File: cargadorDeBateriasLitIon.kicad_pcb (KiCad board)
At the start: 2 copper layers, 17 x 12 mm, 13 parts, among them Q1 2N7002, Q2 2N7002, U1 MCP73831-2, U2 AP9101C

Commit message: PCB version 1, falta probar
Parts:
- added G***: LOGO, MSS_Devices:logo-mr_solder_7.8x3.6mm, B.Cu at (149.0, 105.3)
- added J1: IN+, TestPoint:TestPoint_THTPad_1.5x1.5mm_Drill0.7mm, F.Cu at (140.5, 114.0)
- added J2: IN-, TestPoint:TestPoint_THTPad_1.5x1.5mm_Drill0.7mm, F.Cu at (140.5, 103.0)
- added J3: OUT+, TestPoint:TestPoint_THTPad_1.5x1.5mm_Drill0.7mm, F.Cu at (158.0, 106.0)
- added J4: B+, TestPoint:TestPoint_THTPad_1.5x1.5mm_Drill0.7mm, F.Cu at (158.0, 103.0)
- added J5: B-, TestPoint:TestPoint_THTPad_1.5x1.5mm_Drill0.7mm, F.Cu at (158.0, 111.0)
- added J6: OUT-, TestPoint:TestPoint_THTPad_1.5x1.5mm_Drill0.7mm, F.Cu at (158.0, 114.0)
- moved C1 5.44 mm to (145.7, 112.4), turned to 180 degrees
- moved R2 3.83 mm to (146.5, 105.4), turned to 0 degrees
- moved R1 3.22 mm to (141.6, 108.4), turned to 270 degrees
- moved U2 2.76 mm to (150.7, 108.1)
- moved R3 2.66 mm to (153.3, 107.9)
- moved R4 1.83 mm to (153.7, 105.2)
- moved C3 1.65 mm to (150.4, 105.2)
- moved Q2 1.51 mm to (150.5, 112.1), turned to 270 degrees
- moved Q1 1.29 mm to (154.2, 112.1), turned to 270 degrees
- moved D1 0.88 mm to (146.5, 110.8)
- moved C2 0.84 mm to (143.3, 110.8)
- moved C4 0.67 mm to (143.3, 108.4)
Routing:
- net /B+: track 0.00 -> 24.5 mm
- net /B-: track 0.00 -> 20.5 mm
- net /IN+: track 0.00 -> 10.8 mm
- net Net-(D1-Pad1): track 0.00 -> 9.90 mm
- net GND: track 0.00 -> 8.87 mm, vias 0 -> 1
- net Net-(Q1-Pad3): track 0.00 -> 7.45 mm
- net Net-(R1-Pad1): track 0.00 -> 4.35 mm
- net Net-(Q1-Pad1): track 0.00 -> 4.22 mm
- net Net-(Q1-Pad2): track 0.00 -> 4.02 mm
- net Net-(C3-Pad1): track 0.00 -> 3.61 mm
- net Net-(Q2-Pad1): track 0.00 -> 2.48 mm
- net Net-(R3-Pad2): track 0.00 -> 1.75 mm
- net Net-(R2-Pad2): track 0.00 -> 1.75 mm
- added copper zone on B.Cu, net GND
- added copper zone on F.Cu, net GND
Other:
- board size 17 x 12 mm -> 19.5 x 13 mm
- board text added: "B+"
- board text added: "B-"
- board text added: "IN+"
- board text added: "IN-"
- board text added: "OUT+"
- board text added: "OUT-"

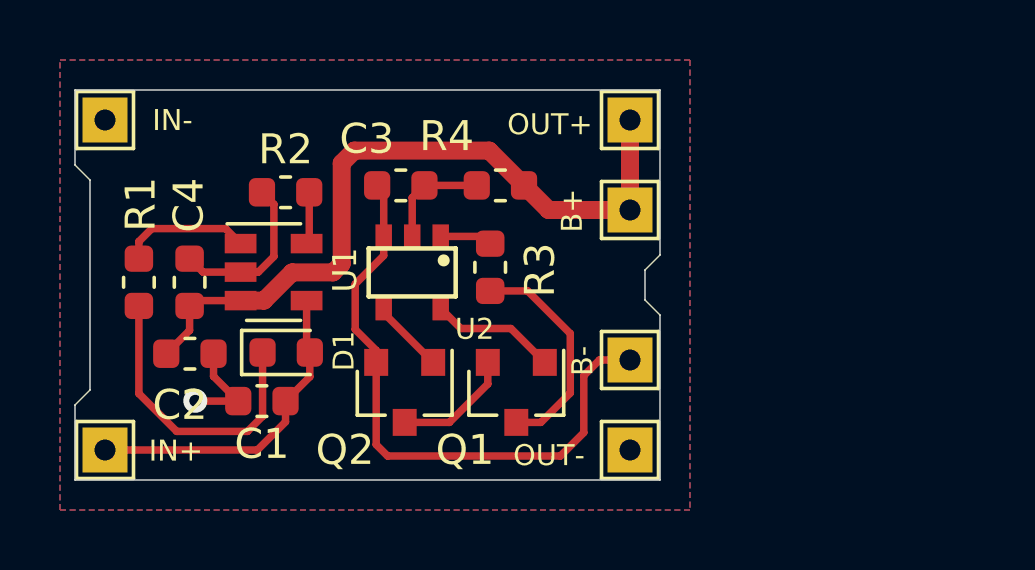
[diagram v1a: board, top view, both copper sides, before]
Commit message: generando gerber, faltan optimizar mas las pistas
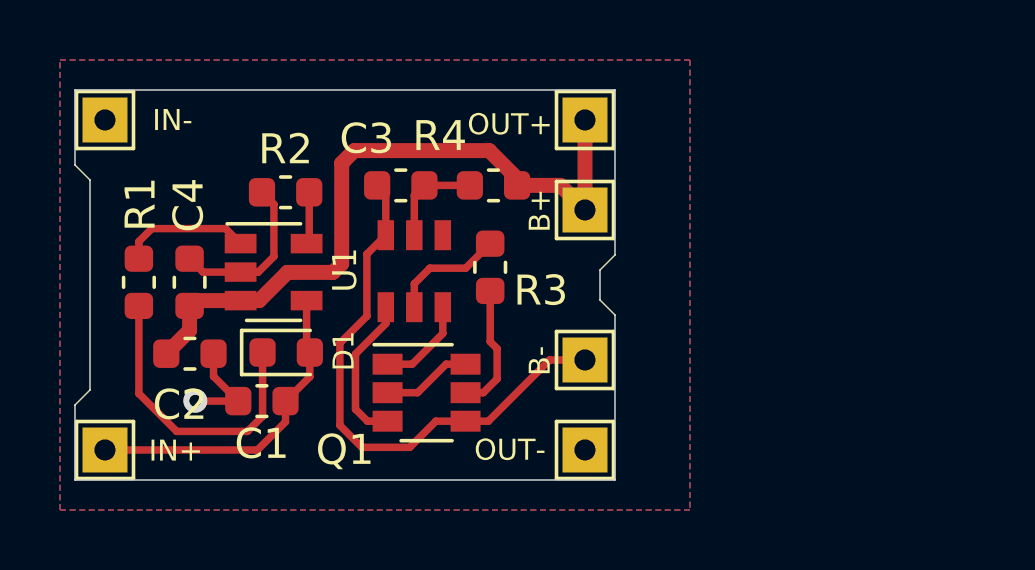
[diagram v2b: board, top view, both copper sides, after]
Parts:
- removed Q2: 2N7002, Package_TO_SOT_SMD:SOT-23
- Q1: value 2N7002 -> FDC6401N; footprint Package_TO_SOT_SMD:SOT-23 -> Package_TO_SOT_SMD:SuperSOT-6
- U1: value MCP73831-2 -> MCP73831
- U2: value AP9101C -> AP9101CK6; footprint MSS_Devices:SOT25 -> MSS_Devices:SOT26
- moved Q1 2.99 mm to (151.2, 112.1), turned to 0 degrees
- moved J3 1.50 mm to (156.5, 106.0)
- moved J4 1.50 mm to (156.5, 103.0)
- moved J5 1.50 mm to (156.5, 111.0)
- moved J6 1.50 mm to (156.5, 114.0)
- moved G*** 1.35 mm to (148.3, 106.5)
- moved R4 0.23 mm to (153.4, 105.2)
- moved U2 0.08 mm to (150.8, 108.0), turned to 0 degrees
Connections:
- R3 pad 1: Net-(Q1-Pad3) -> Net-(Q1-Pad5)
- U2 pad 1: Net-(R3-Pad2) -> Net-(Q1-Pad3)
- U2 pad 2: Net-(C3-Pad1) -> Net-(R3-Pad2)
- U2 pad 3: /B- -> Net-(Q1-Pad1)
- U2 pad 4: Net-(Q2-Pad1) -> (no net)
- U2 pad 5: Net-(Q1-Pad1) -> Net-(C3-Pad1)
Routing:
- net Net-(Q1-Pad5): track 0.00 -> 4.27 mm
- net Net-(Q2-Pad1): track 2.48 -> 0.00 mm
- net Net-(Q1-Pad3): track 7.45 -> 5.05 mm
- net Net-(R3-Pad2): track 1.75 -> 3.86 mm
- net /B-: track 20.5 -> 18.4 mm
- net /B+: track 24.5 -> 23.2 mm
- net Net-(Q1-Pad1): track 4.22 -> 3.14 mm
- net Net-(Q1-Pad2): track 4.02 -> 2.99 mm
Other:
- board size 19.5 x 13 mm -> 18 x 13 mm
- board text added: "MAYKOLREY.COM"

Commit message: agregando fuente de voltaje constante a 5V
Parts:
- removed G***: LOGO, MSS_Devices:logo-mr_solder_7.8x3.6mm
- added C5: 4.7nF, Capacitor_SMD:C_0805_2012Metric, F.Cu at (164.8, 111.5)
- added D2: SM5819PL-TP, Diode_SMD:D_SOD-123F, F.Cu at (164.0, 107.2)
- added L1: 10uH, MSS_Devices:L_Bourns_SDR0403, F.Cu at (159.5, 106.0)
- added R5: 100K, Resistor_SMD:R_0603_1608Metric, F.Cu at (162.0, 110.5)
- added R6: 33K, Resistor_SMD:R_0603_1608Metric, F.Cu at (162.0, 112.2)
- added U3: MIC2251, Package_TO_SOT_SMD:SOT-23-5, F.Cu at (157.8, 111.5)
- C4: value 100nF -> 10uF; footprint Capacitor_SMD:C_0603_1608Metric -> Capacitor_SMD:C_0805_2012Metric
- moved J6 12.0 mm to (168.0, 110.5)
- moved J5 11.9 mm to (168.0, 114.0)
- moved C4 11.7 mm to (154.7, 110.9)
- moved J3 11.5 mm to (168.0, 106.5)
- moved J4 11.5 mm to (168.0, 103.0)
- moved R1 6.81 mm to (147.7, 111.5)
- moved C2 5.83 mm to (144.6, 105.1)
- moved R2 2.94 mm to (147.7, 108.1), turned to 270 degrees
- moved J1 2.06 mm to (142.5, 113.5)
- moved J2 2.00 mm to (142.5, 103.0)
- moved D1 1.24 mm to (145.3, 110.7), turned to 180 degrees
- moved U1 1.13 mm to (145.0, 107.9), turned to 270 degrees
- moved R3 0.91 mm to (154.2, 107.6), turned to 270 degrees
- moved C1 0.44 mm to (145.3, 112.3), turned to 0 degrees
- turned U2 to 180 degrees
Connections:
- net /IN+ renamed VDD
- J3 pad 1: /B+ -> /STEP-UP/VOUT
- Q1 pad 2: Net-(Q1-Pad2) -> GND
- Q1 pad 4: /B- -> Net-(Q1-Pad4)
- Q1 pad 5: Net-(Q1-Pad5) -> /B-
- Q1 pad 6: Net-(Q1-Pad2) -> Net-(Q1-Pad4)
- R3 pad 1: Net-(Q1-Pad5) -> Net-(R3-Pad1)
- R3 pad 2: Net-(R3-Pad2) -> GND
- U2 pad 1: Net-(Q1-Pad3) -> Net-(R3-Pad1)
- U2 pad 2: Net-(R3-Pad2) -> Net-(C3-Pad1)
- U2 pad 3: Net-(Q1-Pad1) -> /B-
- U2 pad 4: (no net) -> Net-(Q1-Pad1)
- U2 pad 5: Net-(C3-Pad1) -> Net-(Q1-Pad3)
- U2 pad 6: /B- -> (no net)
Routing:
- net GND: track 8.87 -> 30.5 mm, vias 1 -> 4
- net Net-(D2-Pad2): track 0.00 -> 10.9 mm, vias 0 -> 4
- net /STEP-UP/VOUT: track 0.00 -> 9.50 mm
- net /B-: track 18.4 -> 27.3 mm
- net Net-(D1-Pad1): track 9.90 -> 2.27 mm
- net /B+: track 23.2 -> 29.0 mm, vias 0 -> 4
- net Net-(Q1-Pad5): track 4.27 -> 0.00 mm
- net Net-(R1-Pad1): track 4.35 -> 8.52 mm
- net Net-(R5-Pad2): track 0.00 -> 4.13 mm
- net Net-(R3-Pad2): track 3.86 -> 0.00 mm
- net Net-(Q1-Pad4): track 0.00 -> 3.31 mm
- net Net-(Q1-Pad2): track 2.99 -> 0.00 mm
- net VDD: track 10.8 -> 7.99 mm
- net Net-(R3-Pad1): track 0.00 -> 2.45 mm
- net Net-(C3-Pad1): track 3.54 -> 5.06 mm
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- added copper zone on B.Cu, net /B+
- added copper zone on F.Cu, net /B+
- added copper zone on B.Cu, net /STEP-UP/VOUT
- added copper zone on F.Cu, net /STEP-UP/VOUT
- added copper zone on B.Cu, net Net-(D2-Pad2)
- added copper zone on F.Cu, net Net-(D2-Pad2)
- added copper zone on F.Cu, net VDD
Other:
- board size 18 x 13 mm -> 27.5 x 13 mm

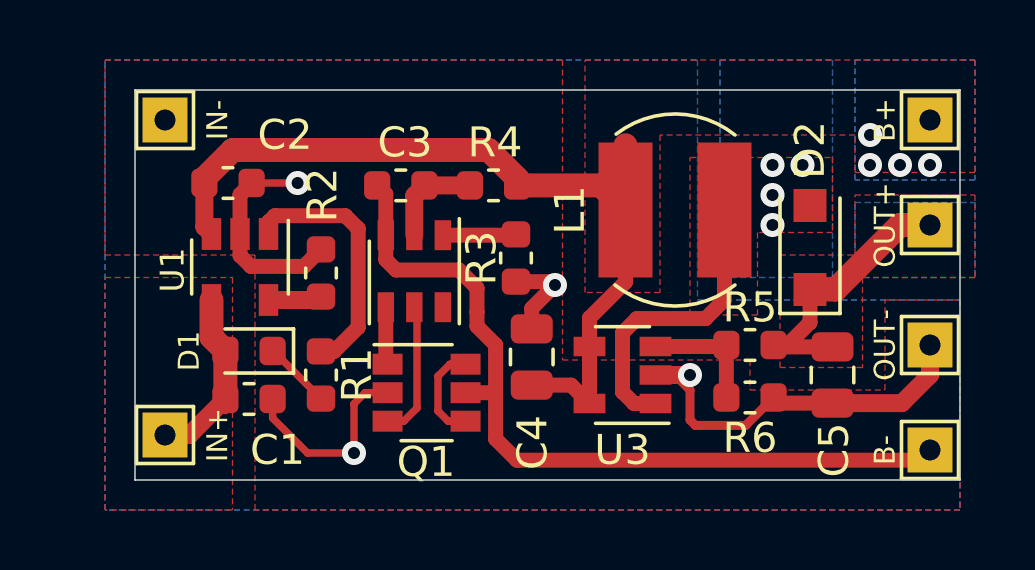
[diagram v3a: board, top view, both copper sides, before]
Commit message: resolviendo error del componente AP9101CK6
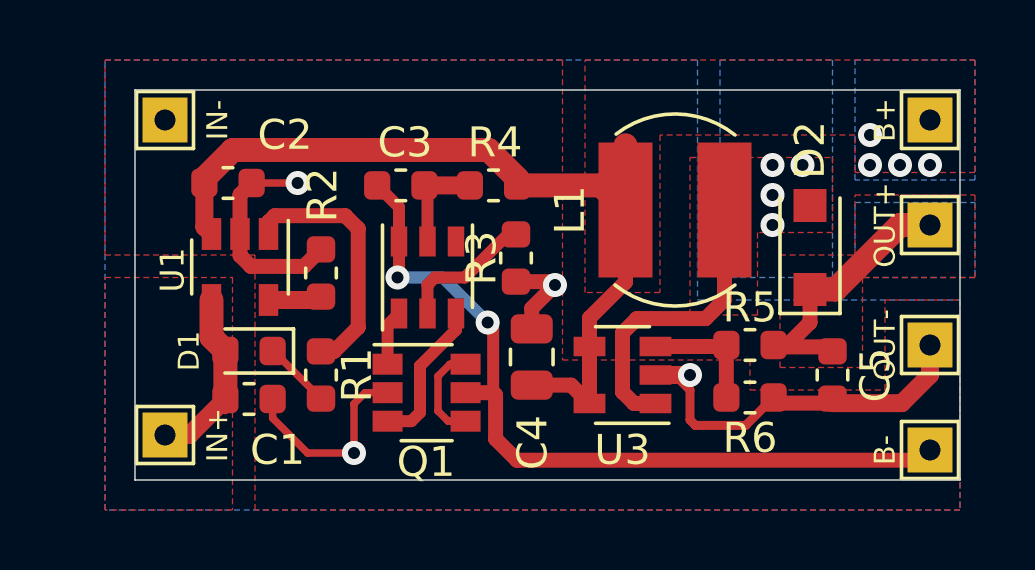
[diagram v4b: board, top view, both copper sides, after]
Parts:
- C5: footprint Capacitor_SMD:C_0805_2012Metric -> Capacitor_SMD:C_0603_1608Metric
- moved U2 0.49 mm to (151.2, 108.2), turned to 0 degrees
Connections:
- U2 pad 1: Net-(R3-Pad1) -> Net-(Q1-Pad1)
- U2 pad 2: Net-(C3-Pad1) -> Net-(R3-Pad1)
- U2 pad 3: /B- -> Net-(Q1-Pad3)
- U2 pad 4: Net-(Q1-Pad1) -> Net-(U2-Pad4)
- U2 pad 5: Net-(Q1-Pad3) -> Net-(C3-Pad1)
- U2 pad 6: (no net) -> /B-
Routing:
- net Net-(R3-Pad1): track 2.45 -> 4.60 mm
- net /B-: track 27.3 -> 26.8 mm, vias 0 -> 2

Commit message: pasado a kicad 6
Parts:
- added G***: LOGO, MSS_Devices:logo-mr_silk, B.Cu at (153.5, 105.5)
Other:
- net class Default removed
